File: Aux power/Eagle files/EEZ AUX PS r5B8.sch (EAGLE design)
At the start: 76 parts, among them IC16 LM25575, IC17 MC7812, IC18 TPD4E002DRLR, IC19 TPD2E001DZDR, IC20 ADUM3160BRWZ, Q20 BTA26-600, Q21 BTA26-600, Q22 IRLL014N, X10 826629-5, X11 2411-01, X4 282836-5, X5 09185067324, X6 22-23-2031, X7 LMJ2138812S0LOT6C, X8 826629-8, X9 826629-5

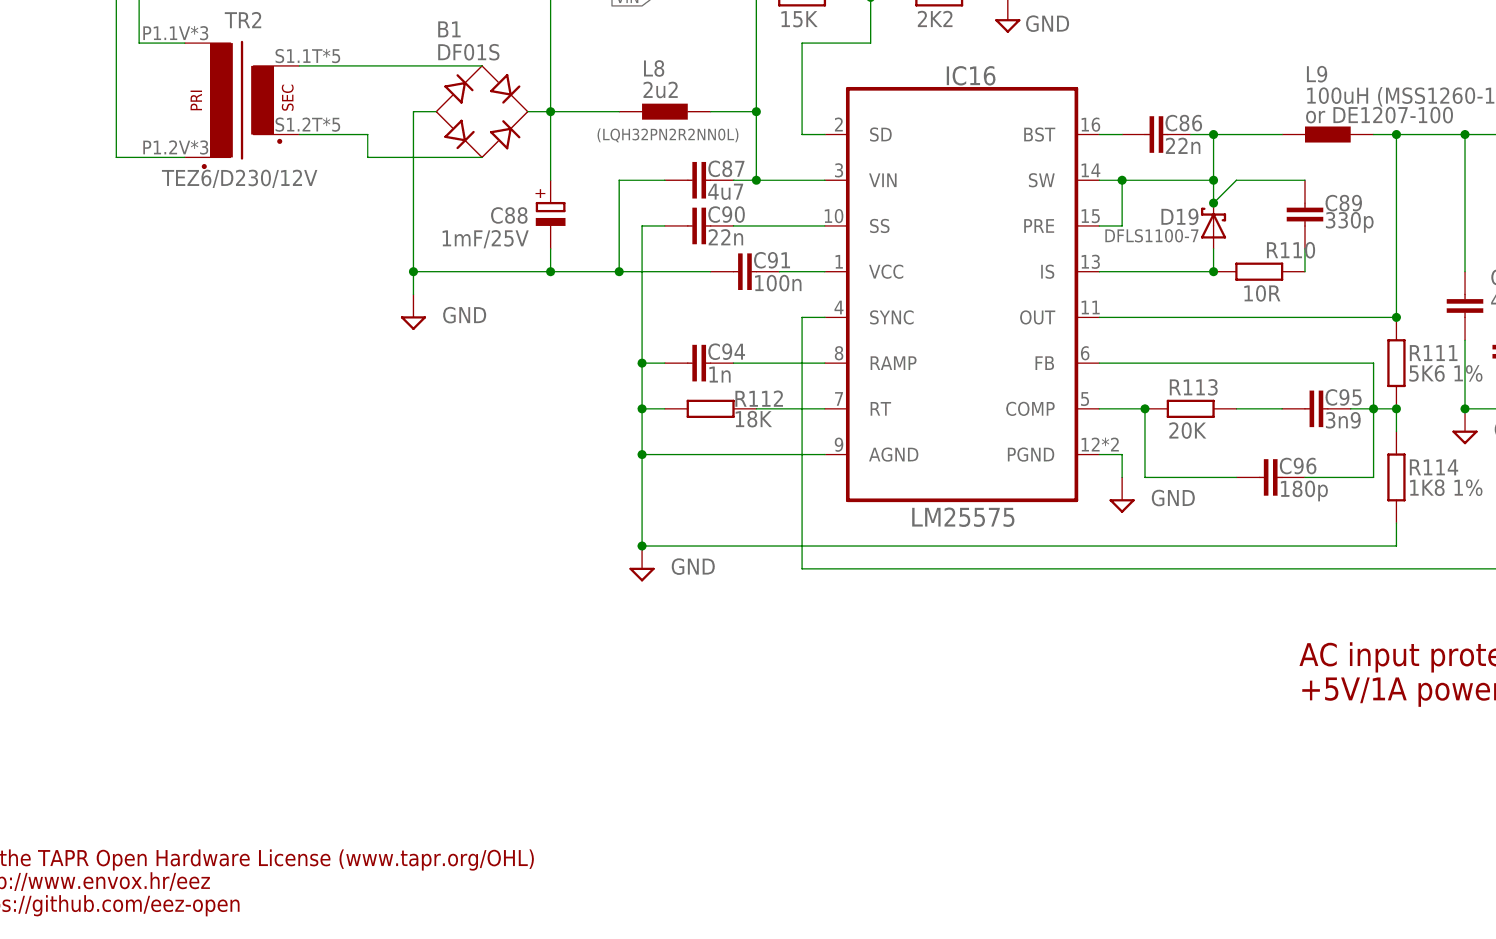
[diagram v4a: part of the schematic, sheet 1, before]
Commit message: PCB fiducials, outlines, milling bridges
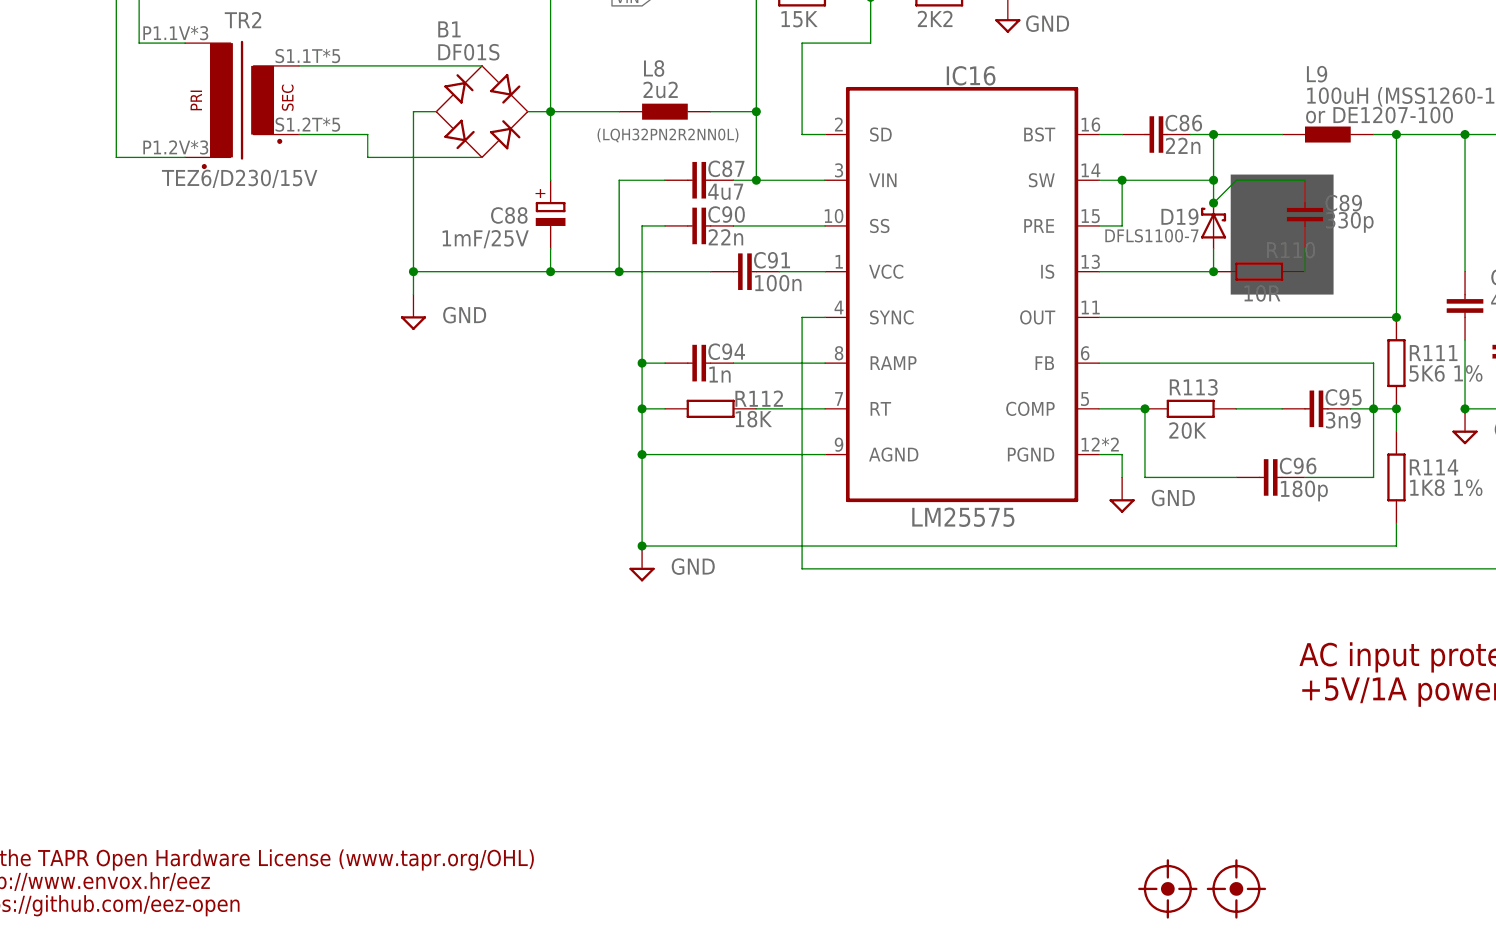
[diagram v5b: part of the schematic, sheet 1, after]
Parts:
- added U$13, U$14: FIDUCIAL_2, EEZ_Lib1:FIDUCIAL_2
- TR2: value TEZ6/D230/12V -> TEZ6/D230/15V
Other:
- note added: "Note 7.1: Mount X4 and X8 on the opposite (top) side of the PCB. Use 14 mm (e.g. Bossard B3X14/BN3320) for enclosure with 3 mm rear panel"
- note removed: "Note 2.1: Mount X4 and X8 on the opposite (top) side of the PCB. Use 14 mm (e.g. Bossard B3X14/BN3320) for enclosure with 3 mm rear panel"
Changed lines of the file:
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@@
 <layer number="112" name="tSilk" color="7" fill="1" visible="no" active="no"/>
 <layer number="113" name="ReferenceLS" color="7" fill="1" visible="yes" active="yes"/>
+<layer number="114" name="EEZ" color="7" fill="1" visible="yes" active="yes"/>
 <layer number="116" name="Patch_BOT" color="7" fill="1" visible="no" active="no"/>
 <layer number="118" name="Rect_Pads" color="7" fill="1" visible="no" active="no"/>
@@
 <part name="R119" library="rcl" deviceset="R-EU_" device="R0805" value="10K"/>
 <part name="SUPPLY51" library="supply2" deviceset="GND" device=""/>
-<part name="TR2" library="EEZ_Lib1" deviceset="PCB_TRAFO6VA_TEZ+VPP" device="+MYRRA" value="TEZ6/D230/12V"/>
+<part name="TR2" library="EEZ_Lib1" deviceset="PCB_TRAFO6VA_TEZ+VPP" device="+MYRRA" value="TEZ6/D230/15V"/>
 <part name="VAR1" library="EEZ_Lib1" deviceset="VARISTOR" device="" value="S20K250"/>
 <part name="VAR2" library="EEZ_Lib1" deviceset="VARISTOR" device="" value="S20K250"/>
@@
 <part name="D21" library="diode" deviceset="DIODE-" device="SOD323-W" value="BAS316"/>
 <part name="C97" library="MyLib6" deviceset="ECAP" device="PANASONIC_C" value="10u"/>
+<part name="U$13" library="EEZ_Lib1" deviceset="FIDUCIAL" device="_2"/>
+<part name="U$14" library="EEZ_Lib1" deviceset="FIDUCIAL" device="_2"/>
 </parts>
 <sheets>
@@
 <text x="233.68" y="118.11" size="1.778" layer="97">Neutral out</text>
 <text x="45.085" y="145.415" size="1.778" layer="96" rot="R180">or 2027-47-BLF</text>
+<rectangle x1="156.845" y1="71.12" x2="168.275" y2="84.455" layer="97"/>
 <text x="86.36" y="88.265" size="1.27" layer="96">(LQH32PN2R2NN0L)</text>
 <polygon width="0.1524" layer="101">
@@
 <text x="6.985" y="176.53" size="1.778" layer="97" rot="MR180">AC input protection and soft-start/stand-by</text>
 <text x="10.16" y="157.48" size="1.778" layer="103">AC input (230V)</text>
-<circle x="232.41" y="67.31" radius="0.635" width="0.1524" layer="101"/>
-<circle x="232.41" y="69.85" radius="0.635" width="0.1524" layer="101"/>
-<text x="230.505" y="70.485" size="1.4224" layer="101" rot="R180">PWR_DIRECT (Input) 3</text>
-<text x="230.505" y="67.945" size="1.4224" layer="101" rot="R180">FAN_SENSE (Output) 5</text>
-<wire x1="236.22" y1="60.96" x2="231.14" y2="60.96" width="0.1524" layer="101"/>
-<wire x1="231.14" y1="60.96" x2="231.14" y2="73.66" width="0.1524" layer="101"/>
-<wire x1="231.14" y1="73.66" x2="236.22" y2="73.66" width="0.1524" layer="101"/>
-<wire x1="236.22" y1="73.66" x2="236.22" y2="60.96" width="0.1524" layer="101"/>
-<circle x="232.41" y="64.77" radius="0.635" width="0.1524" layer="101"/>
-<text x="230.505" y="65.405" size="1.4224" layer="101" rot="R180">Sync (Output) 7</text>
-<circle x="234.95" y="69.85" radius="0.635" width="0.1524" layer="101"/>
-<text x="236.855" y="69.215" size="1.4224" layer="101">4 PWR_SSTART (Input)</text>
-<circle x="234.95" y="67.31" radius="0.635" width="0.1524" layer="101"/>
-<circle x="234.95" y="64.77" radius="0.635" width="0.1524" layer="101"/>
-<text x="236.855" y="66.675" size="1.4224" layer="101">6 FAN_PWM (Input)</text>
-<text x="236.855" y="64.135" size="1.4224" layer="101">8 +5V (Output)</text>
-<circle x="232.41" y="72.39" radius="0.635" width="0.1524" layer="101"/>
-<text x="230.505" y="73.025" size="1.4224" layer="101" rot="R180">Gnd 1</text>
-<circle x="234.95" y="72.39" radius="0.635" width="0.1524" layer="101"/>
-<text x="236.855" y="71.755" size="1.4224" layer="101">2 Gnd</text>
-<circle x="232.41" y="62.23" radius="0.635" width="0.1524" layer="101"/>
-<text x="230.505" y="62.865" size="1.4224" layer="101" rot="R180">Gnd 9</text>
-<circle x="234.95" y="62.23" radius="0.635" width="0.1524" layer="101"/>
-<text x="236.855" y="61.595" size="1.4224" layer="101">10 +5V (Output)</text>
-<text x="2.54" y="154.94" size="1.4224" layer="103">Use e.g. Schurter 4303.6090 IEC inlet</text>
-<text x="2.54" y="152.4" size="1.4224" layer="103">or Schurter KM00.1105.11 IEC intlet</text>
-<text x="2.54" y="149.86" size="1.4224" layer="103">with Schurter 4301.1403 fuse drawer</text>
 <text x="6.985" y="34.925" size="1.6764" layer="103">SAR1</text>
 <text x="6.985" y="19.685" size="1.6764" layer="103">VAR1, VAR2</text>
@@
 <text x="24.13" y="17.145" size="1.6764" layer="103">1.5KE200CA</text>
 <text x="44.45" y="17.145" size="1.6764" layer="103">Farnell: 1837117, TME: 1.5KE200CA</text>
+<circle x="232.41" y="67.31" radius="0.635" width="0.1524" layer="101"/>
+<circle x="232.41" y="69.85" radius="0.635" width="0.1524" layer="101"/>
+<text x="230.505" y="70.485" size="1.4224" layer="101" rot="R180">PWR_DIRECT (Input) 3</text>
+<text x="230.505" y="67.945" size="1.4224" layer="101" rot="R180">FAN_SENSE (Output) 5</text>
+<wire x1="236.22" y1="60.96" x2="231.14" y2="60.96" width="0.1524" layer="101"/>
+<wire x1="231.14" y1="60.96" x2="231.14" y2="73.66" width="0.1524" layer="101"/>
+<wire x1="231.14" y1="73.66" x2="236.22" y2="73.66" width="0.1524" layer="101"/>
+<wire x1="236.22" y1="73.66" x2="236.22" y2="60.96" width="0.1524" layer="101"/>
+<circle x="232.41" y="64.77" radius="0.635" width="0.1524" layer="101"/>
+<text x="230.505" y="65.405" size="1.4224" layer="101" rot="R180">Sync (Output) 7</text>
+<circle x="234.95" y="69.85" radius="0.635" width="0.1524" layer="101"/>
+<text x="236.855" y="69.215" size="1.4224" layer="101">4 PWR_SSTART (Input)</text>
+<circle x="234.95" y="67.31" radius="0.635" width="0.1524" layer="101"/>
+<circle x="234.95" y="64.77" radius="0.635" width="0.1524" layer="101"/>
+<text x="236.855" y="66.675" size="1.4224" layer="101">6 FAN_PWM (Input)</text>
+<text x="236.855" y="64.135" size="1.4224" layer="101">8 +5V (Output)</text>
+<circle x="232.41" y="72.39" radius="0.635" width="0.1524" layer="101"/>
+<text x="230.505" y="73.025" size="1.4224" layer="101" rot="R180">Gnd 1</text>
+<circle x="234.95" y="72.39" radius="0.635" width="0.1524" layer="101"/>
+<text x="236.855" y="71.755" size="1.4224" layer="101">2 Gnd</text>
+<circle x="232.41" y="62.23" radius="0.635" width="0.1524" layer="101"/>
+<text x="230.505" y="62.865" size="1.4224" layer="101" rot="R180">Gnd 9</text>
+<circle x="234.95" y="62.23" radius="0.635" width="0.1524" layer="101"/>
+<text x="236.855" y="61.595" size="1.4224" layer="101">10 +5V (Output)</text>
+<text x="2.54" y="154.94" size="1.4224" layer="103">Use e.g. Schurter 4303.6090 IEC inlet</text>
+<text x="2.54" y="152.4" size="1.4224" layer="103">or Schurter KM00.1105.11 IEC intlet</text>
+<text x="2.54" y="149.86" size="1.4224" layer="103">with Schurter 4301.1403 fuse drawer</text>
 <text x="44.45" y="22.225" size="1.6764" layer="103">Farnell: 2469211</text>
 <text x="44.45" y="32.385" size="1.6764" layer="103">Digikey: 237-1085-ND</text>
@@
 <attribute name="NAME" x="199.39" y="143.891" size="1.778" layer="95"/>
 </instance>
+<instance part="U$13" gate="FD" x="149.86" y="5.08"/>
+<instance part="U$14" gate="FD" x="157.48" y="5.08"/>
 </instances>
 <busses>
@@
 <wire x1="177.8" y1="38.1" x2="177.8" y2="81.28" width="0.1524" layer="97" style="shortdash"/>
 <wire x1="177.8" y1="81.28" x2="157.48" y2="81.28" width="0.1524" layer="97" style="shortdash"/>
-<text x="6.985" y="13.97" size="1.27" layer="103">Note 2.1: Mount X4 and X8 on the opposite (top) side of the PCB. Use 14 mm (e.g. Bossard B3X14/BN3320) for enclosure with 3 mm rear panel</text>
+<text x="6.985" y="13.97" size="1.27" layer="103">Note 7.1: Mount X4 and X8 on the opposite (top) side of the PCB. Use 14 mm (e.g. Bossard B3X14/BN3320) for enclosure with 3 mm rear panel</text>
 <text x="164.465" y="29.845" size="2.54" layer="94" font="vector">Ethernet and USB PCB connectors</text>
 <text x="164.465" y="26.035" size="2.54" layer="94" font="vector">12VDC fan driver (max. 300 mA)</text>
